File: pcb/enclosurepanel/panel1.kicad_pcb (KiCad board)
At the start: 2 copper layers, 60 x 22.7 mm, 0 parts

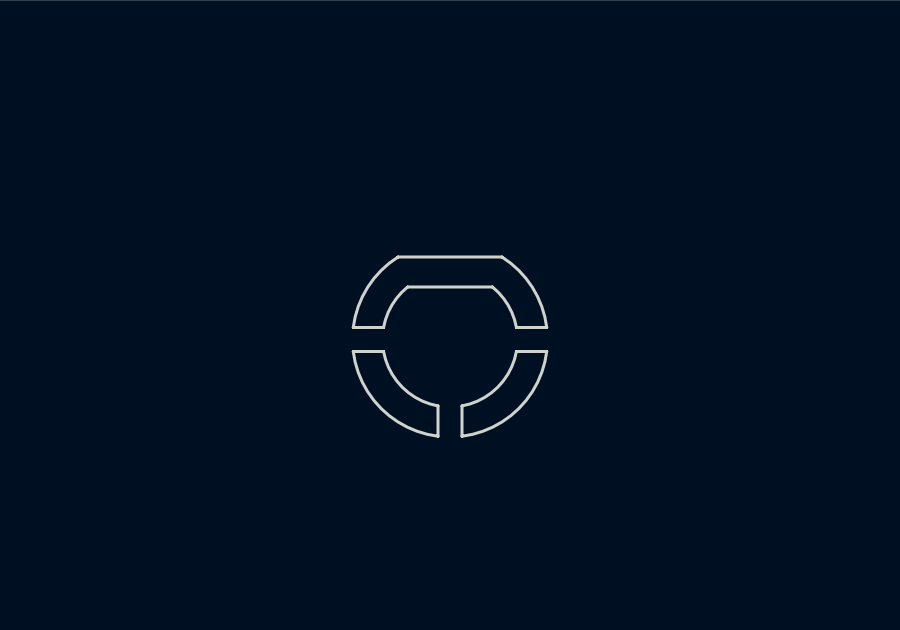
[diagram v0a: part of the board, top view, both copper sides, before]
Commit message: shift the antenna opening in the panel slightly
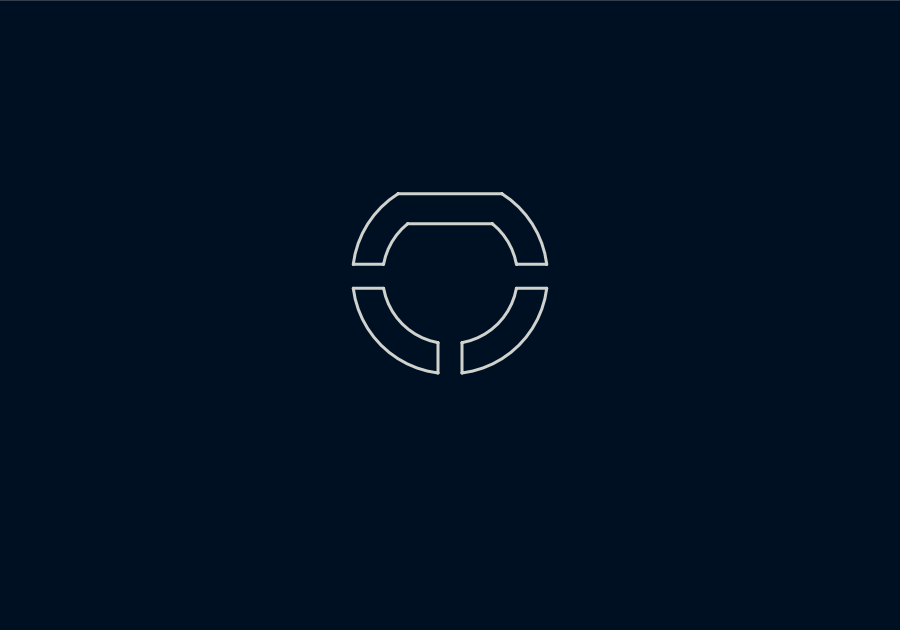
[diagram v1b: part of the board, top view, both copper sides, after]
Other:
- outline, holes or cut-outs redrawn
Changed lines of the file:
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@@
 	(net 0 "")
 	(gr_arc
-		(start 144.751497 78.799246)
-		(mid 143.560514 78.176071)
-		(end 142.937338 76.985087)
-		(stroke
-			(width 0.1)
-			(type default)
-		)
-		(layer "Edge.Cuts")
-	)
-	(gr_line
-		(start 148.376788 76.185087)
-		(end 147.365656 76.185087)
-		(stroke
-			(width 0.1)
-			(type default)
-		)
-		(layer "Edge.Cuts")
-	)
-	(gr_line
-		(start 145.551497 79.810378)
-		(end 145.551497 78.799246)
-		(stroke
-			(width 0.1)
-			(type default)
-		)
-		(layer "Edge.Cuts")
-	)
-	(gr_arc
-		(start 146.883548 73.835087)
-		(mid 147.894567 74.842082)
-		(end 148.376788 76.185087)
-		(stroke
-			(width 0.1)
-			(type default)
-		)
-		(layer "Edge.Cuts")
-	)
-	(gr_arc
-		(start 148.376788 76.985087)
-		(mid 147.449594 78.883185)
-		(end 145.551497 79.810378)
-		(stroke
-			(width 0.1)
-			(type default)
-		)
-		(layer "Edge.Cuts")
-	)
-	(gr_line
-		(start 146.56571 74.835087)
-		(end 143.737283 74.835087)
+		(start 144.751497 76.690926)
+		(mid 143.560483 76.067766)
+		(end 142.937338 74.876767)
+		(stroke
+			(width 0.1)
+			(type default)
+		)
+		(layer "Edge.Cuts")
+	)
+	(gr_line
+		(start 148.376788 74.076767)
+		(end 147.365656 74.076767)
+		(stroke
+			(width 0.1)
+			(type default)
+		)
+		(layer "Edge.Cuts")
+	)
+	(gr_line
+		(start 145.551497 77.702058)
+		(end 145.551497 76.690926)
+		(stroke
+			(width 0.1)
+			(type default)
+		)
+		(layer "Edge.Cuts")
+	)
+	(gr_arc
+		(start 146.883548 71.726767)
+		(mid 147.894572 72.73376)
+		(end 148.376788 74.076767)
+		(stroke
+			(width 0.1)
+			(type default)
+		)
+		(layer "Edge.Cuts")
+	)
+	(gr_arc
+		(start 148.376788 74.876767)
+		(mid 147.449598 76.77487)
+		(end 145.551497 77.702058)
+		(stroke
+			(width 0.1)
+			(type default)
+		)
+		(layer "Edge.Cuts")
+	)
+	(gr_line
+		(start 146.56571 72.726767)
+		(end 143.737283 72.726767)
 		(stroke
 			(width 0.1)
@@
 	)
 	(gr_arc
-		(start 141.926206 76.185087)
-		(mid 142.408418 74.842073)
-		(end 143.419446 73.835087)
-		(stroke
-			(width 0.1)
-			(type default)
-		)
-		(layer "Edge.Cuts")
-	)
-	(gr_arc
-		(start 146.56571 74.835087)
-		(mid 147.087188 75.438089)
-		(end 147.365656 76.185087)
-		(stroke
-			(width 0.1)
-			(type default)
-		)
-		(layer "Edge.Cuts")
-	)
-	(gr_arc
-		(start 144.751497 79.810378)
-		(mid 142.853399 78.883185)
-		(end 141.926206 76.985087)
+		(start 141.926206 74.076767)
+		(mid 142.408409 72.733749)
+		(end 143.419446 71.726767)
+		(stroke
+			(width 0.1)
+			(type default)
+		)
+		(layer "Edge.Cuts")
+	)
+	(gr_arc
+		(start 146.56571 72.726767)
+		(mid 147.087191 73.329768)
+		(end 147.365656 74.076767)
+		(stroke
+			(width 0.1)
+			(type default)
+		)
+		(layer "Edge.Cuts")
+	)
+	(gr_arc
+		(start 144.751497 77.702058)
+		(mid 142.853405 76.774862)
+		(end 141.926206 74.876767)
 		(stroke
 			(width 0.1)
@@
 	)
 	(gr_line
-		(start 142.937338 76.185087)
-		(end 141.926206 76.185087)
+		(start 142.937338 74.076767)
+		(end 141.926206 74.076767)
 		(stroke
 			(width 0.1)
@@
 	)
 	(gr_line
-		(start 141.926206 76.985087)
-		(end 142.937338 76.985087)
+		(start 141.926206 74.876767)
+		(end 142.937338 74.876767)
 		(stroke
 			(width 0.1)
@@
 	)
 	(gr_arc
-		(start 147.365656 76.985087)
-		(mid 146.742479 78.17606)
-		(end 145.551497 78.799246)
+		(start 147.365656 74.876767)
+		(mid 146.742473 76.067745)
+		(end 145.551497 76.690926)
 		(stroke
 			(width 0.1)
@@
 	)
 	(gr_line
-		(start 144.751497 78.799246)
-		(end 144.751497 79.810378)
-		(stroke
-			(width 0.1)
-			(type default)
-		)
-		(layer "Edge.Cuts")
-	)
-	(gr_line
-		(start 147.365656 76.985087)
-		(end 148.376788 76.985087)
+		(start 144.751497 76.690926)
+		(end 144.751497 77.702058)
+		(stroke
+			(width 0.1)
+			(type default)
+		)
+		(layer "Edge.Cuts")
+	)
+	(gr_line
+		(start 147.365656 74.876767)
+		(end 148.376788 74.876767)
 		(stroke
 			(width 0.1)
@@
 	)
 	(gr_line
-		(start 143.419446 73.835087)
-		(end 146.883548 73.835087)
+		(start 143.419446 71.726767)
+		(end 146.883548 71.726767)
 		(stroke
 			(width 0.1)
@@
 	)
 	(gr_arc
-		(start 142.937338 76.185087)
-		(mid 143.215799 75.438083)
-		(end 143.737283 74.835087)
-		(stroke
-			(width 0.1)
+		(start 142.937338 74.076767)
+		(mid 143.215793 73.32976)
+		(end 143.737283 72.726767)
+		(stroke
+			(width 0.1)

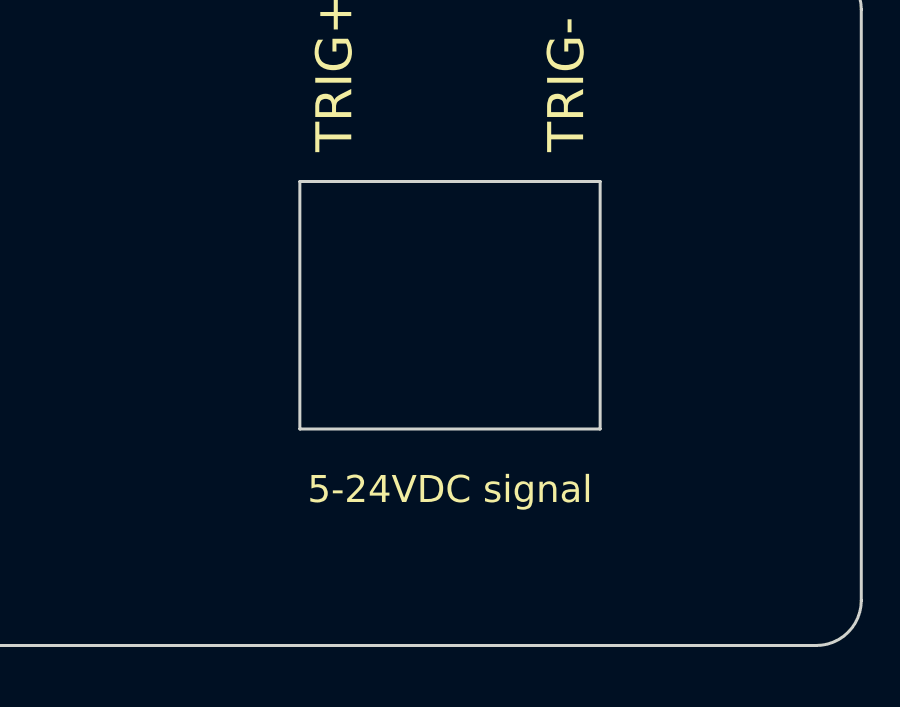
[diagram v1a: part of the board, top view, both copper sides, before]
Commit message: Add protection diode to opto, increase pulldown strength
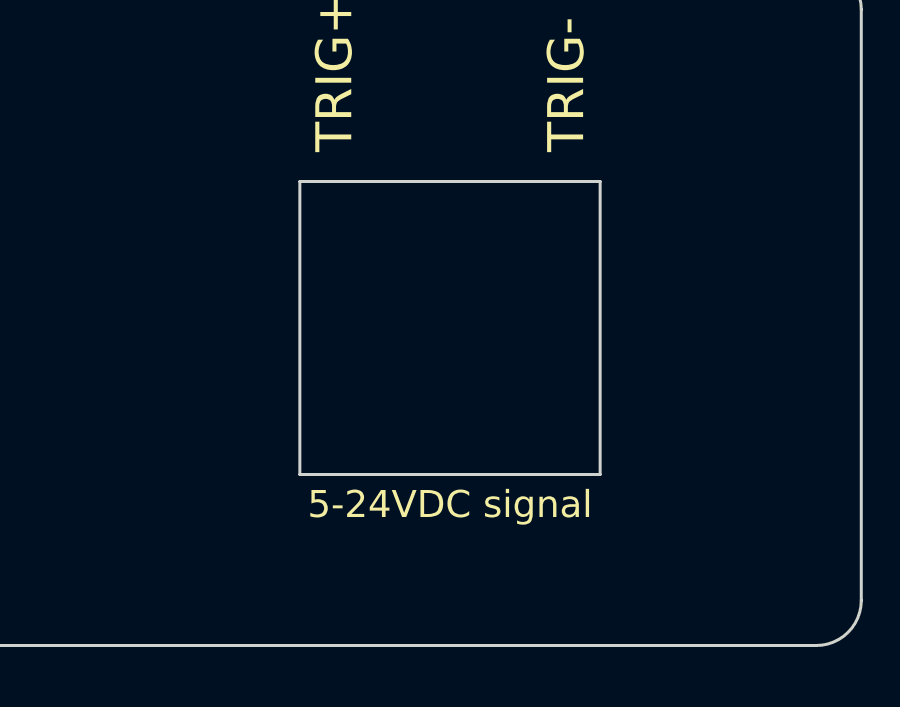
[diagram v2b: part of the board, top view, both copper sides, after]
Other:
- outline, holes or cut-outs redrawn
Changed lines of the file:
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@@
 	)
 	(gr_line
-		(start 163.344848 80.710087)
+		(start 163.344848 82.226767)
 		(end 163.344848 72.460087)
 		(stroke
@@
 	(gr_line
 		(start 173.354848 72.460087)
-		(end 173.354848 80.710087)
+		(end 173.354848 82.226767)
 		(stroke
 			(width 0.1)
@@
 	)
 	(gr_line
-		(start 173.354848 80.710087)
-		(end 163.344848 80.710087)
+		(start 173.354848 82.226767)
+		(end 163.344848 82.226767)
 		(stroke
 			(width 0.1)
@@
 	)
 	(gr_text "5-24VDC signal\n"
-		(at 168.349848 82.726767 0)
+		(at 168.349848 83.226767 0)
 		(layer "F.SilkS")
 		(effects

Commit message: fixup
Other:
- outline, holes or cut-outs redrawn
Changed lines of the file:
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@@
 (kicad_pcb
-	(version 20240108)
+	(version 20241229)
 	(generator "pcbnew")
-	(generator_version "8.0")
+	(generator_version "9.0")
 	(general
 		(thickness 1.6)
@@
 	(layers
 		(0 "F.Cu" signal)
-		(31 "B.Cu" signal)
-		(32 "B.Adhes" user "B.Adhesive")
-		(33 "F.Adhes" user "F.Adhesive")
-		(34 "B.Paste" user)
-		(35 "F.Paste" user)
-		(36 "B.SilkS" user "B.Silkscreen")
-		(37 "F.SilkS" user "F.Silkscreen")
-		(38 "B.Mask" user)
-		(39 "F.Mask" user)
-		(40 "Dwgs.User" user "User.Drawings")
-		(41 "Cmts.User" user "User.Comments")
-		(42 "Eco1.User" user "User.Eco1")
-		(43 "Eco2.User" user "User.Eco2")
-		(44 "Edge.Cuts" user)
-		(45 "Margin" user)
-		(46 "B.CrtYd" user "B.Courtyard")
-		(47 "F.CrtYd" user "F.Courtyard")
-		(48 "B.Fab" user)
-		(49 "F.Fab" user)
-		(50 "User.1" user)
-		(51 "User.2" user)
-		(52 "User.3" user)
-		(53 "User.4" user)
-		(54 "User.5" user)
-		(55 "User.6" user)
-		(56 "User.7" user)
-		(57 "User.8" user)
-		(58 "User.9" user)
+		(2 "B.Cu" signal)
+		(9 "F.Adhes" user "F.Adhesive")
+		(11 "B.Adhes" user "B.Adhesive")
+		(13 "F.Paste" user)
+		(15 "B.Paste" user)
+		(5 "F.SilkS" user "F.Silkscreen")
+		(7 "B.SilkS" user "B.Silkscreen")
+		(1 "F.Mask" user)
+		(3 "B.Mask" user)
+		(17 "Dwgs.User" user "User.Drawings")
+		(19 "Cmts.User" user "User.Comments")
+		(21 "Eco1.User" user "User.Eco1")
+		(23 "Eco2.User" user "User.Eco2")
+		(25 "Edge.Cuts" user)
+		(27 "Margin" user)
+		(31 "F.CrtYd" user "F.Courtyard")
+		(29 "B.CrtYd" user "B.Courtyard")
+		(35 "F.Fab" user)
+		(33 "B.Fab" user)
+		(39 "User.1" user)
+		(41 "User.2" user)
+		(43 "User.3" user)
+		(45 "User.4" user)
+		(47 "User.5" user)
+		(49 "User.6" user)
+		(51 "User.7" user)
+		(53 "User.8" user)
+		(55 "User.9" user)
 	)
 	(setup
 		(pad_to_mask_clearance 0)
 		(allow_soldermask_bridges_in_footprints no)
+		(tenting front back)
 		(aux_axis_origin 122.059225 87.726767)
 		(grid_origin 122.059225 87.726767)
 		(pcbplotparams
-			(layerselection 0x00010fc_ffffffff)
-			(plot_on_all_layers_selection 0x0000000_00000000)
+			(layerselection 0x00000000_00000000_55555555_5755f5ff)
+			(plot_on_all_layers_selection 0x00000000_00000000_00000000_00000000)
 			(disableapertmacros no)
 			(usegerberextensions no)
@@
 			(svgprecision 4)
 			(plotframeref no)
-			(viasonmask no)
 			(mode 1)
 			(useauxorigin no)
@@
 			(pdf_front_fp_property_popups yes)
 			(pdf_back_fp_property_popups yes)
+			(pdf_metadata yes)
+			(pdf_single_document no)
 			(dxfpolygonmode yes)
 			(dxfimperialunits yes)
@@
 			(psnegative no)
 			(psa4output no)
-			(plotreference yes)
-			(plotvalue yes)
-			(plotfptext yes)
-			(plotinvisibletext no)
+			(plot_black_and_white yes)
 			(sketchpadsonfab no)
+			(plotpadnumbers no)
+			(hidednponfab no)
+			(sketchdnponfab yes)
+			(crossoutdnponfab yes)
 			(subtractmaskfromsilk no)
 			(outputformat 1)
@@
 	(net 0 "")
 	(gr_arc
-		(start 144.751497 76.690926)
-		(mid 143.560483 76.067766)
-		(end 142.937338 74.876767)
-		(stroke
-			(width 0.1)
-			(type default)
-		)
-		(layer "Edge.Cuts")
-	)
-	(gr_line
-		(start 148.376788 74.076767)
-		(end 147.365656 74.076767)
-		(stroke
-			(width 0.1)
-			(type default)
-		)
-		(layer "Edge.Cuts")
-	)
-	(gr_line
-		(start 145.551497 77.702058)
-		(end 145.551497 76.690926)
-		(stroke
-			(width 0.1)
-			(type default)
-		)
-		(layer "Edge.Cuts")
-	)
-	(gr_arc
-		(start 146.883548 71.726767)
-		(mid 147.894572 72.73376)
-		(end 148.376788 74.076767)
-		(stroke
-			(width 0.1)
-			(type default)
-		)
-		(layer "Edge.Cuts")
-	)
-	(gr_arc
-		(start 148.376788 74.876767)
-		(mid 147.449598 76.77487)
-		(end 145.551497 77.702058)
-		(stroke
-			(width 0.1)
-			(type default)
-		)
-		(layer "Edge.Cuts")
-	)
-	(gr_line
-		(start 146.56571 72.726767)
-		(end 143.737283 72.726767)
+		(start 132.861124 76.690926)
+		(mid 131.67011 76.067766)
+		(end 131.046965 74.876767)
+		(stroke
+			(width 0.1)
+			(type default)
+		)
+		(layer "Edge.Cuts")
+	)
+	(gr_line
+		(start 136.486415 74.076767)
+		(end 135.475283 74.076767)
+		(stroke
+			(width 0.1)
+			(type default)
+		)
+		(layer "Edge.Cuts")
+	)
+	(gr_line
+		(start 133.661124 77.702058)
+		(end 133.661124 76.690926)
+		(stroke
+			(width 0.1)
+			(type default)
+		)
+		(layer "Edge.Cuts")
+	)
+	(gr_arc
+		(start 134.993175 71.726767)
+		(mid 136.004175 72.733768)
+		(end 136.486415 74.076767)
+		(stroke
+			(width 0.1)
+			(type default)
+		)
+		(layer "Edge.Cuts")
+	)
+	(gr_arc
+		(start 136.486415 74.876767)
+		(mid 135.559225 76.77487)
+		(end 133.661124 77.702058)
+		(stroke
+			(width 0.1)
+			(type default)
+		)
+		(layer "Edge.Cuts")
+	)
+	(gr_line
+		(start 134.675337 72.726767)
+		(end 131.84691 72.726767)
 		(stroke
 			(width 0.1)
@@
 	)
 	(gr_arc
-		(start 141.926206 74.076767)
-		(mid 142.408409 72.733749)
-		(end 143.419446 71.726767)
-		(stroke
-			(width 0.1)
-			(type default)
-		)
-		(layer "Edge.Cuts")
-	)
-	(gr_arc
-		(start 146.56571 72.726767)
-		(mid 147.087191 73.329768)
-		(end 147.365656 74.076767)
-		(stroke
-			(width 0.1)
-			(type default)
-		)
-		(layer "Edge.Cuts")
-	)
-	(gr_arc
-		(start 144.751497 77.702058)
-		(mid 142.853405 76.774862)
-		(end 141.926206 74.876767)
+		(start 130.035833 74.076767)
+		(mid 130.518022 72.733738)
+		(end 131.529073 71.726767)
+		(stroke
+			(width 0.1)
+			(type default)
+		)
+		(layer "Edge.Cuts")
+	)
+	(gr_arc
+		(start 134.675337 72.726767)
+		(mid 135.196818 73.329768)
+		(end 135.475283 74.076767)
+		(stroke
+			(width 0.1)
+			(type default)
+		)
+		(layer "Edge.Cuts")
+	)
+	(gr_arc
+		(start 132.861124 77.702058)
+		(mid 130.963032 76.774862)
+		(end 130.035833 74.876767)
 		(stroke
 			(width 0.1)
@@
 	)
 	(gr_line
-		(start 142.937338 74.076767)
-		(end 141.926206 74.076767)
+		(start 131.046965 74.076767)
+		(end 130.035833 74.076767)
 		(stroke
 			(width 0.1)
@@
 	)
 	(gr_line
-		(start 141.926206 74.876767)
-		(end 142.937338 74.876767)
+		(start 130.035833 74.876767)
+		(end 131.046965 74.876767)
 		(stroke
 			(width 0.1)
@@
 	)
 	(gr_arc
-		(start 147.365656 74.876767)
-		(mid 146.742473 76.067745)
-		(end 145.551497 76.690926)
+		(start 135.475283 74.876767)
+		(mid 134.8521 76.067745)
+		(end 133.661124 76.690926)
 		(stroke
 			(width 0.1)
@@
 	)
 	(gr_line
-		(start 144.751497 76.690926)
-		(end 144.751497 77.702058)
-		(stroke
-			(width 0.1)
-			(type default)
-		)
-		(layer "Edge.Cuts")
-	)
-	(gr_line
-		(start 147.365656 74.876767)
-		(end 148.376788 74.876767)
+		(start 132.861124 76.690926)
+		(end 132.861124 77.702058)
+		(stroke
+			(width 0.1)
+			(type default)
+		)
+		(layer "Edge.Cuts")
+	)
+	(gr_line
+		(start 135.475283 74.876767)
+		(end 136.486415 74.876767)
 		(stroke
 			(width 0.1)
@@
 	)
 	(gr_line
-		(start 143.419446 71.726767)
-		(end 146.883548 71.726767)
+		(start 131.529073 71.726767)
+		(end 134.993175 71.726767)
 		(stroke
 			(width 0.1)
@@
 	)
 	(gr_arc
-		(start 142.937338 74.076767)
-		(mid 143.215793 73.32976)
-		(end 143.737283 72.726767)
-		(stroke
-			(width 0.1)
-			(type default)
-		)
-		(layer "Edge.Cuts")
+		(start 131.046965 74.076767)
+		(mid 131.32542 73.32976)
+		(end 131.84691 72.726767)
+		(stroke
+			(width 0.1)
+			(type default)
+		)
+		(layer "Edge.Cuts")
+	)
+	(gr_text "5-24VDC signal\n"
+		(at 168.349848 83.226767 0)
+		(layer "F.SilkS")
+		(effects
+			(font
+				(size 0.9 0.9)
+				(thickness 0.13)
+			)
+		)
+	)
+	(gr_text "TRIG+\n\n\n\nTRIG-"
+		(at 163.801233 71.476767 90)
+		(layer "F.SilkS" knockout)
+		(effects
+			(font
+				(size 1.2 1.2)
+				(thickness 0.15)
+			)
+			(justify left top)
+		)
 	)
 	(gr_text "cncvac"
@@
 		)
 	)
-	(gr_text "5-24VDC signal\n"
-		(at 168.349848 83.226767 0)
-		(layer "F.SilkS")
-		(effects
-			(font
-				(size 0.9 0.9)
-				(thickness 0.13)
-			)
-		)
-	)
-	(gr_text "TRIG+\n\n\n\nTRIG-"
-		(at 163.801233 71.476767 90)
-		(layer "F.SilkS" knockout)
-		(effects
-			(font
-				(size 1.2 1.2)
-				(thickness 0.15)
-			)
-			(justify left top)
-		)
-	)
+	(embedded_fonts no)
 )
